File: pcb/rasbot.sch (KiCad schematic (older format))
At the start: 0 parts

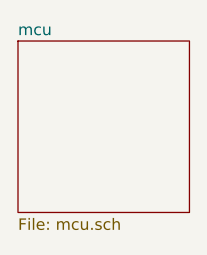
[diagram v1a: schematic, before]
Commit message: [PCB & Firmware] Motors PWM Signal MCU Pins
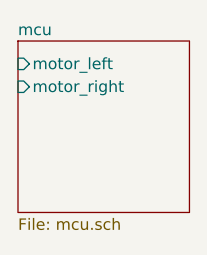
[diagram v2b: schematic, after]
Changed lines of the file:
@@
 F0 "mcu" 50
 F1 "mcu.sch" 50
+F2 "motor_left" I L 5200 3300 50
+F3 "motor_right" I L 5200 3400 50
 $EndSheet
 $EndSCHEMATC

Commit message: [PCB & Firmware] Line Sensors MCU Pins
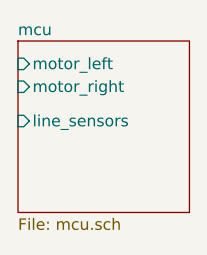
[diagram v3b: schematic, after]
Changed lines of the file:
@@
 F2 "motor_left" I L 5200 3300 50
 F3 "motor_right" I L 5200 3400 50
+F4 "line_sensors" I L 5200 3550 50
 $EndSheet
 $EndSCHEMATC

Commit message: [PCB & Firmware] I2C for LCD SSD1306 MCU Pins
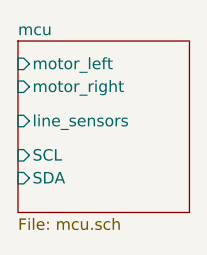
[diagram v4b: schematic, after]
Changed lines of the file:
@@
 F3 "motor_right" I L 5200 3400 50
 F4 "line_sensors" I L 5200 3550 50
+F5 "SCL" I L 5200 3700 50
+F6 "SDA" I L 5200 3800 50
 $EndSheet
 $EndSCHEMATC

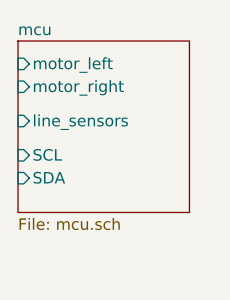
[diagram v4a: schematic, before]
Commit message: [PCB & Firmware] Light Sensor MCU Pin
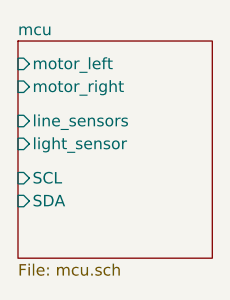
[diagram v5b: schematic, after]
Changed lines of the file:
@@
 $EndDescr
 $Sheet
-S 5200 3200 750  750
+S 5200 3200 850  950
 U 5D0ADCD4
 F0 "mcu" 50
@@
 F3 "motor_right" I L 5200 3400 50
 F4 "line_sensors" I L 5200 3550 50
-F5 "SCL" I L 5200 3700 50
-F6 "SDA" I L 5200 3800 50
+F5 "SCL" I L 5200 3800 50
+F6 "SDA" I L 5200 3900 50
+F7 "light_sensor" I L 5200 3650 50
 $EndSheet
 $EndSCHEMATC

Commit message: IR matrix
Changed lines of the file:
@@
 $Descr A4 11693 8268
 encoding utf-8
-Sheet 1 2
+Sheet 1 17
 Title ""
 Date ""
@@
 F0 "mcu" 50
 F1 "mcu.sch" 50
-F2 "motor_left" I L 5200 3300 50
-F3 "motor_right" I L 5200 3400 50
-F4 "line_sensors" I L 5200 3550 50
-F5 "SCL" I L 5200 3800 50
-F6 "SDA" I L 5200 3900 50
-F7 "light_sensor" I L 5200 3650 50
+$EndSheet
+$Sheet
+S 7100 3200 1150 1400
+U 5D1373A3
+F0 "sensors" 50
+F1 "sensors.sch" 50
+F2 "IR_row1" I L 7100 3400 50
+F3 "IR_row2" I L 7100 3500 50
+F4 "IR_row0" I L 7100 3300 50
+F5 "IR_row3" I L 7100 3600 50
+F6 "IR_row4" I L 7100 3700 50
+F7 "IR_row5" I L 7100 3800 50
+F8 "IR_row6" I L 7100 3900 50
 $EndSheet
 $EndSCHEMATC

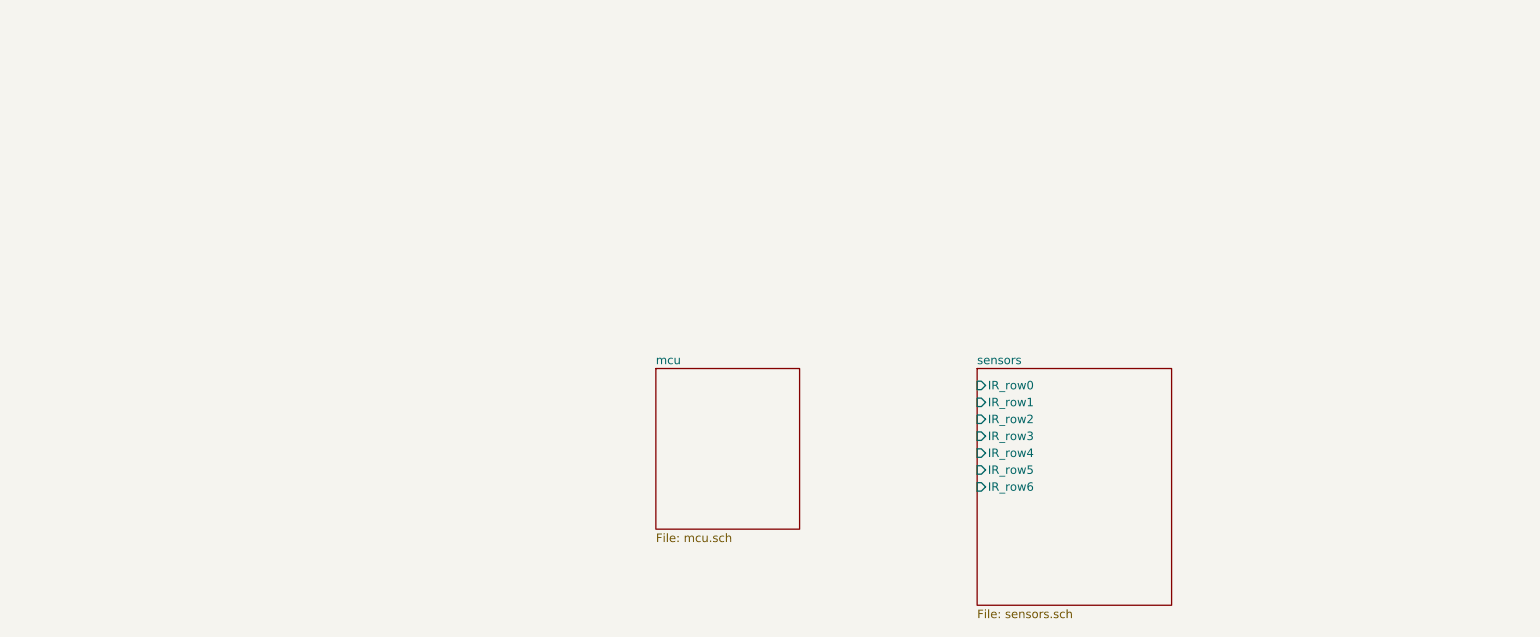
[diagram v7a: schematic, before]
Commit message: Use Buses for IR sensors
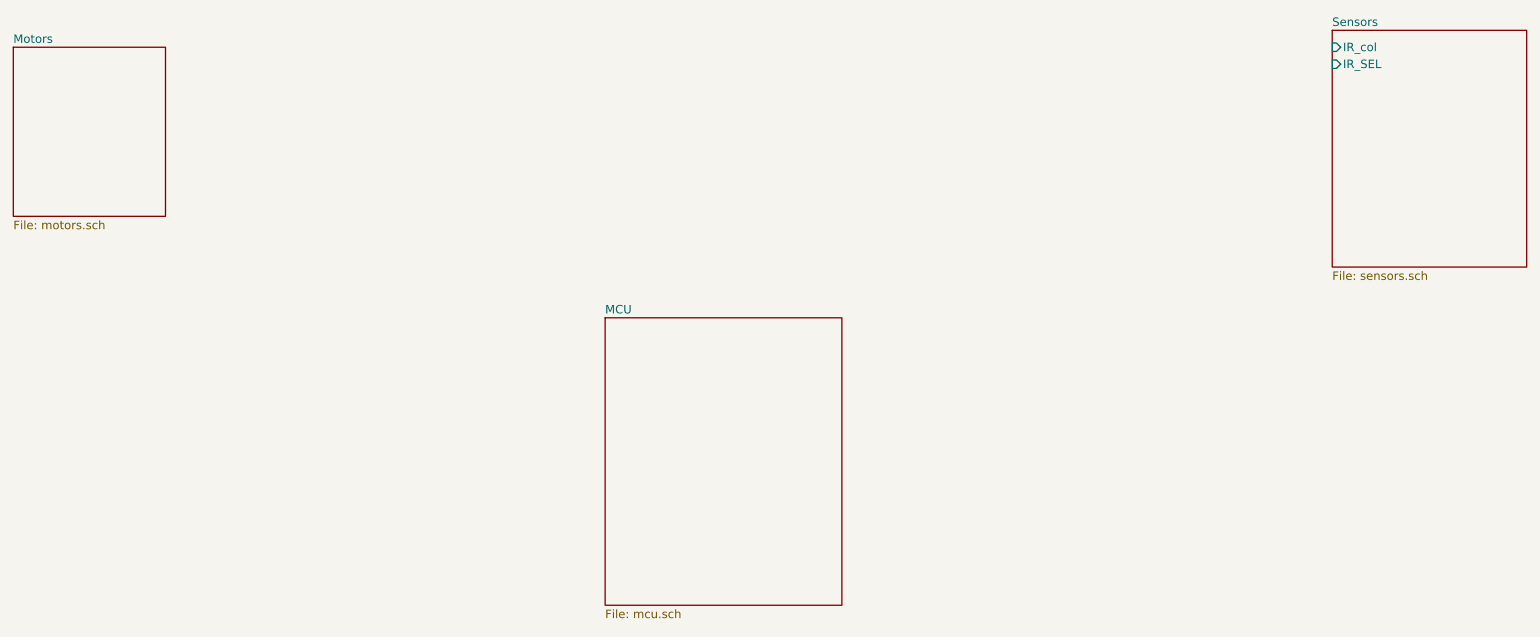
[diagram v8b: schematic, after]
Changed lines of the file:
@@
 $Descr A4 11693 8268
 encoding utf-8
-Sheet 1 17
+Sheet 1 19
 Title ""
 Date ""
@@
 $EndDescr
 $Sheet
-S 5200 3200 850  950
+S 4900 2900 1400 1700
 U 5D0ADCD4
-F0 "mcu" 50
+F0 "MCU" 50
 F1 "mcu.sch" 50
 $EndSheet
 $Sheet
-S 7100 3200 1150 1400
+S 9200 1200 1150 1400
 U 5D1373A3
-F0 "sensors" 50
+F0 "Sensors" 50
 F1 "sensors.sch" 50
-F2 "IR_row1" I L 7100 3400 50
-F3 "IR_row2" I L 7100 3500 50
-F4 "IR_row0" I L 7100 3300 50
-F5 "IR_row3" I L 7100 3600 50
-F6 "IR_row4" I L 7100 3700 50
-F7 "IR_row5" I L 7100 3800 50
-F8 "IR_row6" I L 7100 3900 50
+F2 "IR_col" I L 9200 1300 50
+F3 "IR_SEL" I L 9200 1400 50
+$EndSheet
+$Sheet
+S 1400 1300 900  1000
+U 5D25A1F3
+F0 "Motors" 50
+F1 "motors.sch" 50
 $EndSheet
 $EndSCHEMATC
